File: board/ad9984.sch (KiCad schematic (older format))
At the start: 26 parts, among them U401 AD9984

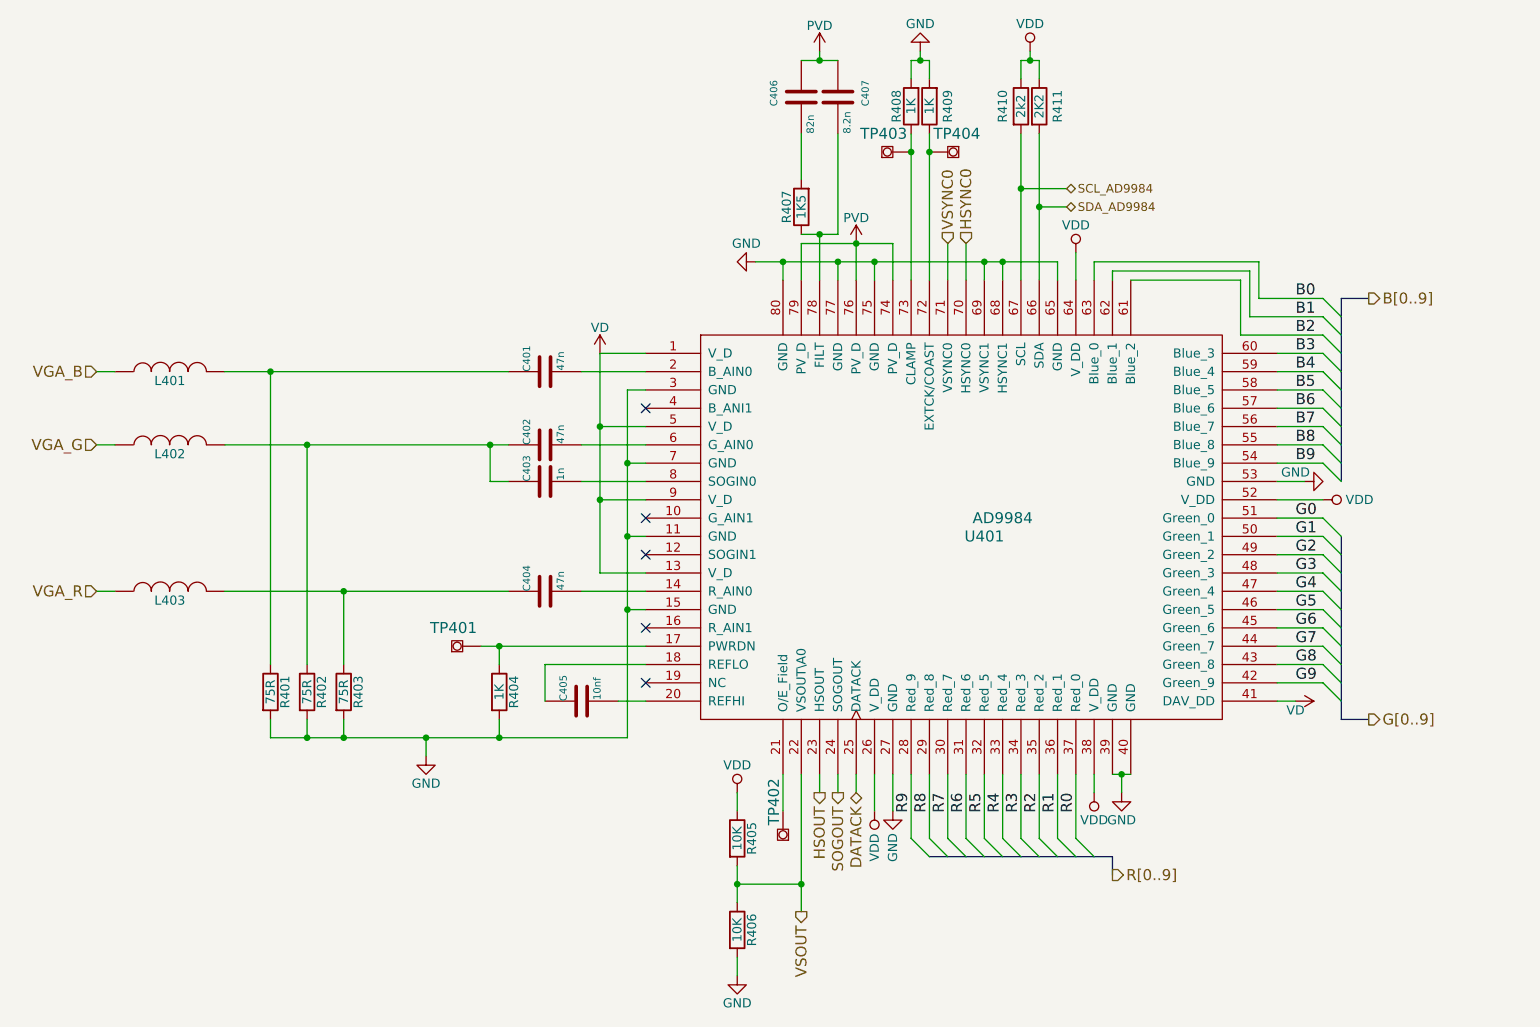
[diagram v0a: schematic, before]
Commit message: Add component inputs for AD9984 secondardy inputs
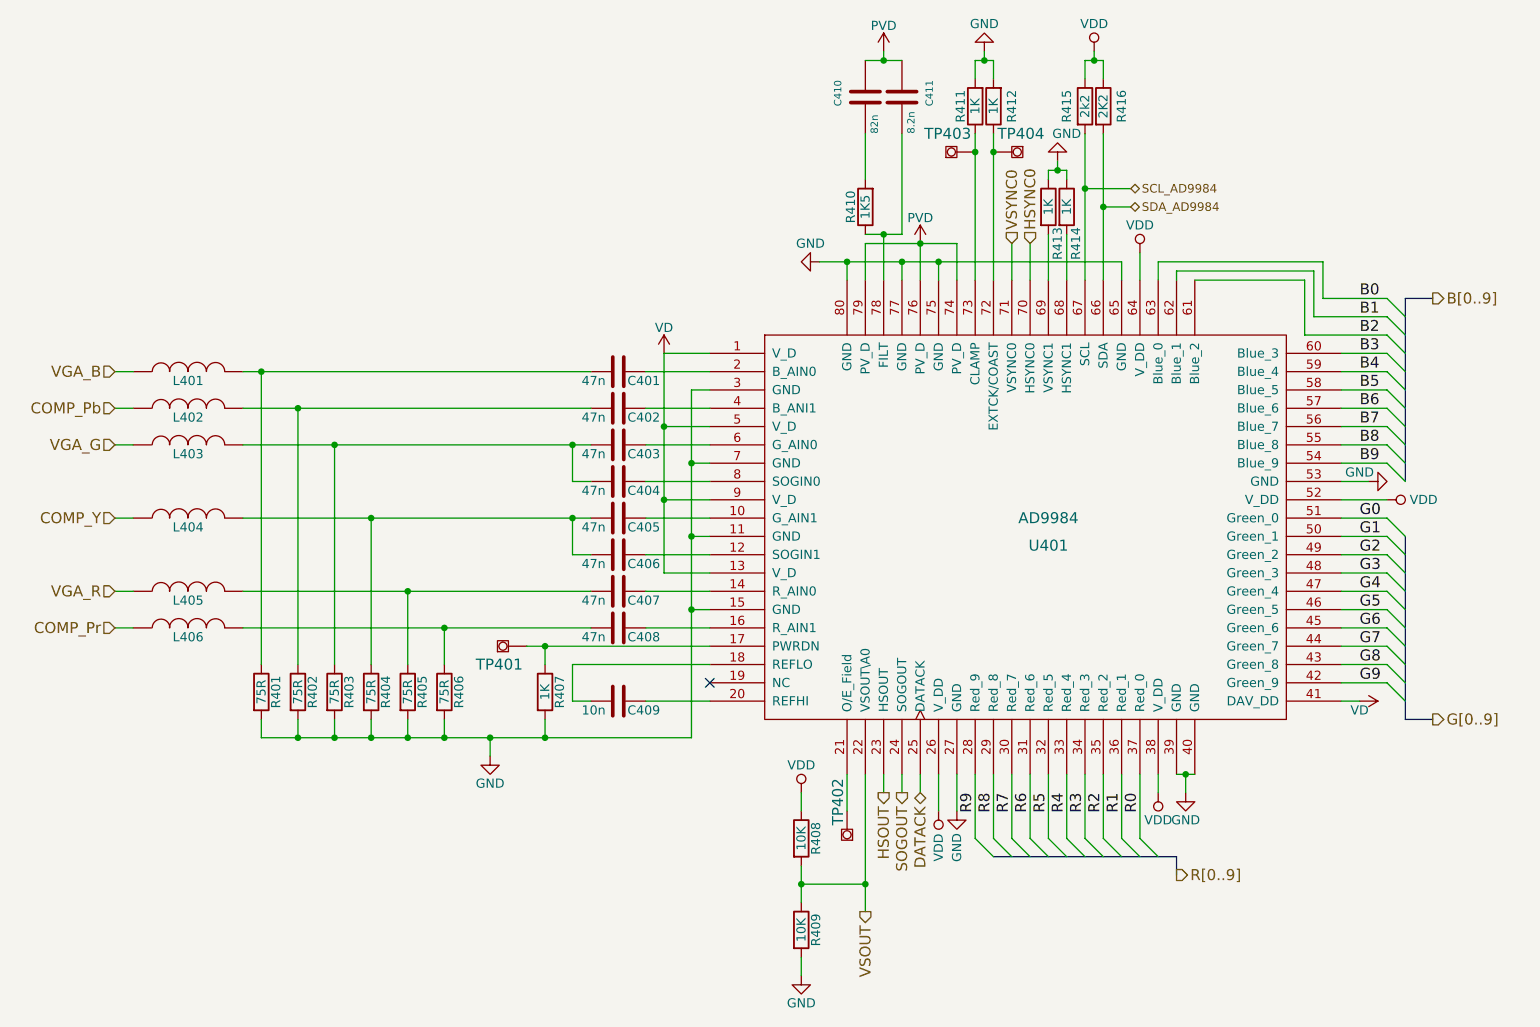
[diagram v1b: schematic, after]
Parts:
- removed C401, C402, C404: 47n, ~, symbol C-RESCUE-vgaExp
- removed C403: 1n, ~, symbol C-RESCUE-vgaExp
- removed C405: 10nf, ~, symbol C-RESCUE-vgaExp
- added C401, C402, C403, C404, C405, C406, C407, C408: 47n, symbol C
- added C409: 10n, symbol C
- added L402, L404, L406: FERRITE, symbol INDUCTOR
- added R401, R402, R406: 75R, symbol R
- added R413, R414: 1K, symbol R
- renumbered C406 to C410, C407 to C411, L402 to L403, L403 to L405, R401 to R403, R402 to R404, R403 to R405, R404 to R407, R405 to R408, R406 to R409, R407 to R410, R408 to R411, R409 to R412, R410 to R415, R411 to R416
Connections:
- net GND: now also R401.2, R402.2, R406.2, R413.1, R414.1; no longer U401.68 (HSYNC1), U401.69 (VSYNC1)
- net at U401.10 (G_AIN1): now also C405.1
- net at U401.12 (SOGIN1): now also C406.1
- net at U401.14 (R_AIN0): now also C407.1
- net at U401.16 (R_AIN1): now also C408.1
- net at U401.18 (REFLO): now also C409.2
- net at U401.2 (B_AIN0): now also C401.1
- net at U401.20 (REFHI): now also C409.1
- net at U401.4 (B_ANI1): now also C402.1
- net at U401.6 (G_AIN0): now also C403.1
- net at U401.8 (SOGIN0): now also C404.1
- net at R403.1: now also L403.2, C403.2, C404.2; no longer L401.2
- net at R404.1: now also C405.2, C406.2, L404.2; no longer L403.2
- net at L405.2, R405.1: now also C407.2
- new net: R414.2, U401.68 (HSYNC1)
- new net: R413.2, U401.69 (VSYNC1)
- new net: C401.2, L401.2, R401.1
- new net: C408.2, L406.2, R406.1
- new net: C402.2, L402.2, R402.1
- new net COMP_Pb: L402.1
- new net COMP_Pr: L406.1
- new net COMP_Y: L404.1
- no-connect marks 5 -> 1
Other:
- moved on the sheet: C410, C411, L401, L403, L405, R403, R404, R405, R407, R408, R409, R410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

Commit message: Add I2C headers
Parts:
- added P401: AD9984 I2C, symbol CONN_01X04
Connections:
- net GND: now also P401.4 (P4)
- net SCL_AD9984: now also P401.2 (P2)
- net SDA_AD9984: now also P401.3 (P3)
- net VDD: now also P401.1 (P1)
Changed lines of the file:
@@
 $EndComp
 $Comp
-L VDD #PWR418
+L VDD #PWR419
 U 1 1 5641327C
 P 9100 3650
-F 0 "#PWR418" H 9100 3500 50  0001 C CNN
+F 0 "#PWR419" H 9100 3500 50  0001 C CNN
 F 1 "VDD" V 9100 3850 50  0000 C CNN
 F 2 "" H 9100 3650 60  0000 C CNN
@@
 Connection ~ 6150 2350
 $Comp
-L VD #PWR416
+L VD #PWR417
 U 1 1 56416F9D
 P 8950 4750
-F 0 "#PWR416" H 8950 4600 50  0001 C CNN
+F 0 "#PWR417" H 8950 4600 50  0001 C CNN
 F 1 "VD" V 9000 4750 50  0000 C CNN
 F 2 "" H 8950 4750 60  0000 C CNN
@@
 $EndComp
 $Comp
-L GND #PWR417
+L GND #PWR418
 U 1 1 564170A0
 P 9000 3550
-F 0 "#PWR417" H 9000 3300 50  0001 C CNN
+F 0 "#PWR418" H 9000 3300 50  0001 C CNN
 F 1 "GND" V 9050 3600 50  0000 C CNN
 F 2 "" H 9000 3550 60  0000 C CNN
@@
 	1    0    0    -1
 $EndComp
-Text HLabel 7700 2050 2    47   BiDi ~ 0
+Text HLabel 8250 2050 2    47   BiDi ~ 0
 SDA_AD9984
-Text HLabel 7700 1950 2    47   BiDi ~ 0
+Text HLabel 8250 1950 2    47   BiDi ~ 0
 SCL_AD9984
 Wire Wire Line
-	7700 1950 7450 1950
-Wire Wire Line
-	7550 2050 7700 2050
+	7450 1950 8250 1950
+Wire Wire Line
+	7550 2050 8250 2050
 Connection ~ 7550 2050
 Connection ~ 7450 1950
@@
 	4500 4850 4500 4950
 Connection ~ 4500 4950
+$Comp
+L CONN_01X04 P401
+U 1 1 5692F854
+P 8000 1600
+F 0 "P401" H 8000 1850 50  0000 C CNN
+F 1 "AD9984 I2C" V 8100 1600 50  0000 C CNN
+F 2 "" H 8000 1600 50  0000 C CNN
+F 3 "" H 8000 1600 50  0000 C CNN
+	1    8000 1600
+	0    -1   -1   0
+$EndComp
+$Comp
+L GND #PWR416
+U 1 1 5692FBEE
+P 8250 1850
+F 0 "#PWR416" H 8250 1600 50  0001 C CNN
+F 1 "GND" V 8250 1650 50  0000 C CNN
+F 2 "" H 8250 1850 50  0000 C CNN
+F 3 "" H 8250 1850 50  0000 C CNN
+	1    8250 1850
+	0    -1   -1   0
+$EndComp
+Wire Wire Line
+	7850 1800 7850 2300
+Wire Wire Line
+	7850 2300 7750 2300
+Wire Wire Line
+	8150 1800 8150 1850
+Wire Wire Line
+	8150 1850 8250 1850
+Wire Wire Line
+	7950 1800 7950 1950
+Connection ~ 7950 1950
+Wire Wire Line
+	8050 1800 8050 2050
+Connection ~ 8050 2050
 $EndSCHEMATC

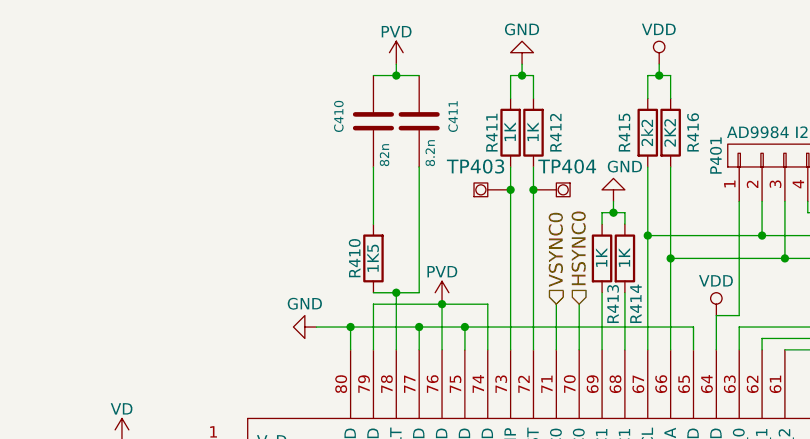
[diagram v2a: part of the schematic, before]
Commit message: Start assigning footprints
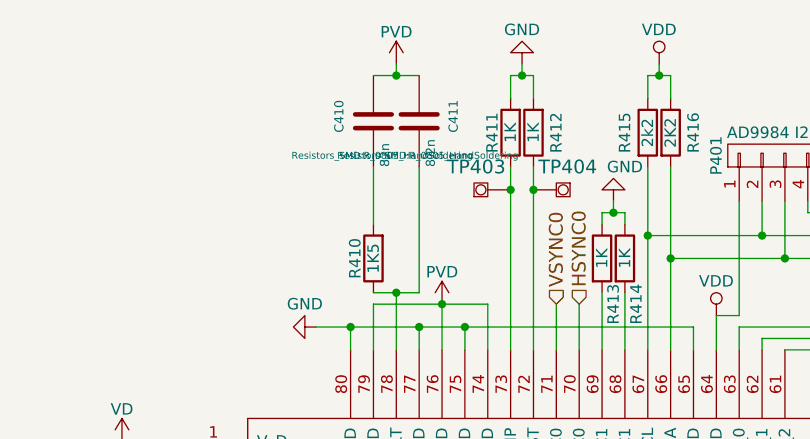
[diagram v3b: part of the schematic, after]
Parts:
- C401, C402, C403, C404, C405, C406, C407, C408, C409, L401, L402, L403, L404, L405, L406, R401, R402, R403, R404, R405, R406, R407, R408, R409, R410, R411, R412, R413, R414, R415, R416: footprint (none) -> Resistors_SMD:R_0805_HandSoldering
- C410, C411: footprint ~ -> Resistors_SMD:R_0805_HandSoldering
- U401: footprint ~ -> (none)

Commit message: More footprint assigning and generated Netlist
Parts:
- U401: footprint (none) -> analog-devices2:analog-devices2-LQFP80
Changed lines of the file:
@@
 F 0 "U401" H 7250 3700 60  0000 C CNN
 F 1 "AD9984" H 7250 3850 60  0000 C CNN
-F 2 "" H 6350 4050 60  0001 C CNN
+F 2 "analog-devices2:analog-devices2-LQFP80" H 6350 4050 60  0001 C CNN
 F 3 "~" H 6350 4050 60  0000 C CNN
 	1    7150 3800

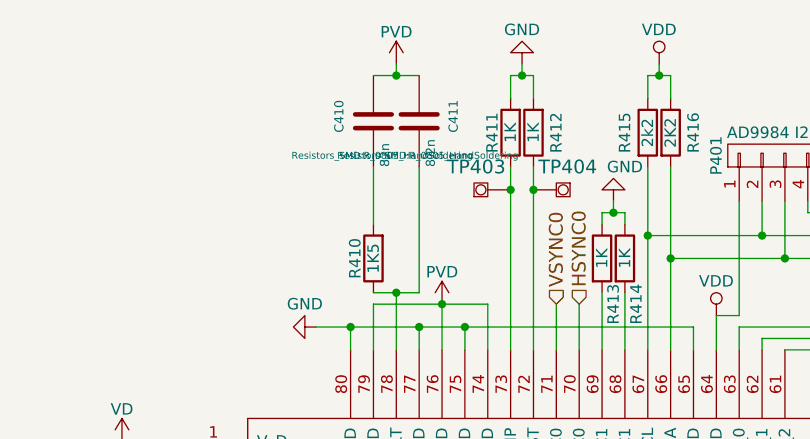
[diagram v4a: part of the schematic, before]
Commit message: More footprint assigning
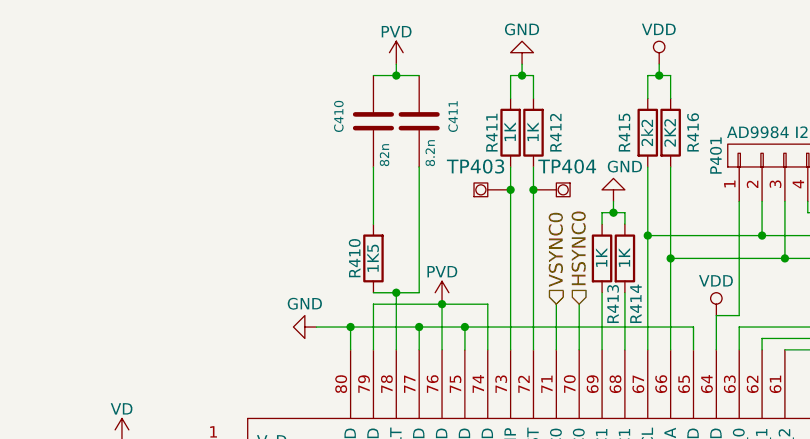
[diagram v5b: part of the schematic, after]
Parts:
- P401: footprint (none) -> CON-4X1-2.54:CON-2X1-2.54
- TP401, TP402, TP403, TP404: footprint (none) -> SMD_Packages:1Pin
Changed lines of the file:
@@
 F 0 "C410" V 6100 1400 40  0000 L CNN
 F 1 "82n" V 6300 1250 40  0000 L CNN
-F 2 "Resistors_SMD:R_0805_HandSoldering" H 6288 1300 30  0000 C CNN
+F 2 "Resistors_SMD:R_0805_HandSoldering" H 6288 1300 30  0001 C CNN
 F 3 "~" H 6250 1450 60  0000 C CNN
 	1    6250 1450
@@
 F 0 "C411" V 6600 1400 40  0000 L CNN
 F 1 "8.2n" V 6500 1250 40  0000 L CNN
-F 2 "Resistors_SMD:R_0805_HandSoldering" H 6488 1300 30  0000 C CNN
+F 2 "Resistors_SMD:R_0805_HandSoldering" H 6488 1300 30  0001 C CNN
 F 3 "~" H 6450 1450 60  0000 C CNN
 	1    6450 1450
@@
 F 0 "TP402" V 6200 5300 60  0000 C CNN
 F 1 "TESTPOINT" H 6150 5300 60  0001 C CNN
-F 2 "" H 6150 5350 60  0001 C CNN
+F 2 "SMD_Packages:1Pin" H 6150 5350 60  0001 C CNN
 F 3 "" H 6150 5350 60  0000 C CNN
 	1    6150 5350
@@
 F 0 "TP401" V 4300 4600 60  0000 C CNN
 F 1 "TESTPOINT" H 4400 4400 60  0001 C CNN
-F 2 "" H 4400 4450 60  0001 C CNN
+F 2 "SMD_Packages:1Pin" H 4400 4450 60  0001 C CNN
 F 3 "" H 4400 4450 60  0000 C CNN
 	1    4400 4450
@@
 F 0 "TP404" V 6850 1900 60  0000 C CNN
 F 1 "TESTPOINT" H 6950 1700 60  0001 C CNN
-F 2 "" H 6950 1750 60  0001 C CNN
+F 2 "SMD_Packages:1Pin" H 6950 1750 60  0001 C CNN
 F 3 "" H 6950 1750 60  0000 C CNN
 	1    6950 1750
@@
 F 0 "TP403" V 6950 1900 60  0000 C CNN
 F 1 "TESTPOINT" H 6850 1700 60  0001 C CNN
-F 2 "" H 6850 1750 60  0001 C CNN
+F 2 "SMD_Packages:1Pin" H 6850 1750 60  0001 C CNN
 F 3 "" H 6850 1750 60  0000 C CNN
 	1    6850 1750
@@
 F 0 "P401" H 8000 1850 50  0000 C CNN
 F 1 "AD9984 I2C" V 8100 1600 50  0000 C CNN
-F 2 "" H 8000 1600 50  0001 C CNN
+F 2 "CON-4X1-2.54:CON-2X1-2.54" H 8000 1600 50  0001 C CNN
 F 3 "" H 8000 1600 50  0000 C CNN
 	1    8000 1600

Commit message: Finish footprint assignment
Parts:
- P401: footprint CON-4X1-2.54:CON-2X1-2.54 -> CON-SMD-2.54:HARWIN-M20-87-4x1
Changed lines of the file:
@@
 F 0 "P401" H 8000 1850 50  0000 C CNN
 F 1 "AD9984 I2C" V 8100 1600 50  0000 C CNN
-F 2 "CON-4X1-2.54:CON-2X1-2.54" H 8000 1600 50  0001 C CNN
+F 2 "CON-SMD-2.54:HARWIN-M20-87-4x1" H 8000 1600 50  0001 C CNN
 F 3 "" H 8000 1600 50  0000 C CNN
 	1    8000 1600
